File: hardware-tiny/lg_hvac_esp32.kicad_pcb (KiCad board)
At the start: 4 copper layers, 29 x 50.3 mm, 15 parts, among them J1 JST_XH_S3B-XH-A-1_01x03, J2 Conn_01x19_Female_1_to_19, J3 Conn_01x19_Female_20_to_38, U1 TPS82130, U2 TJA1027

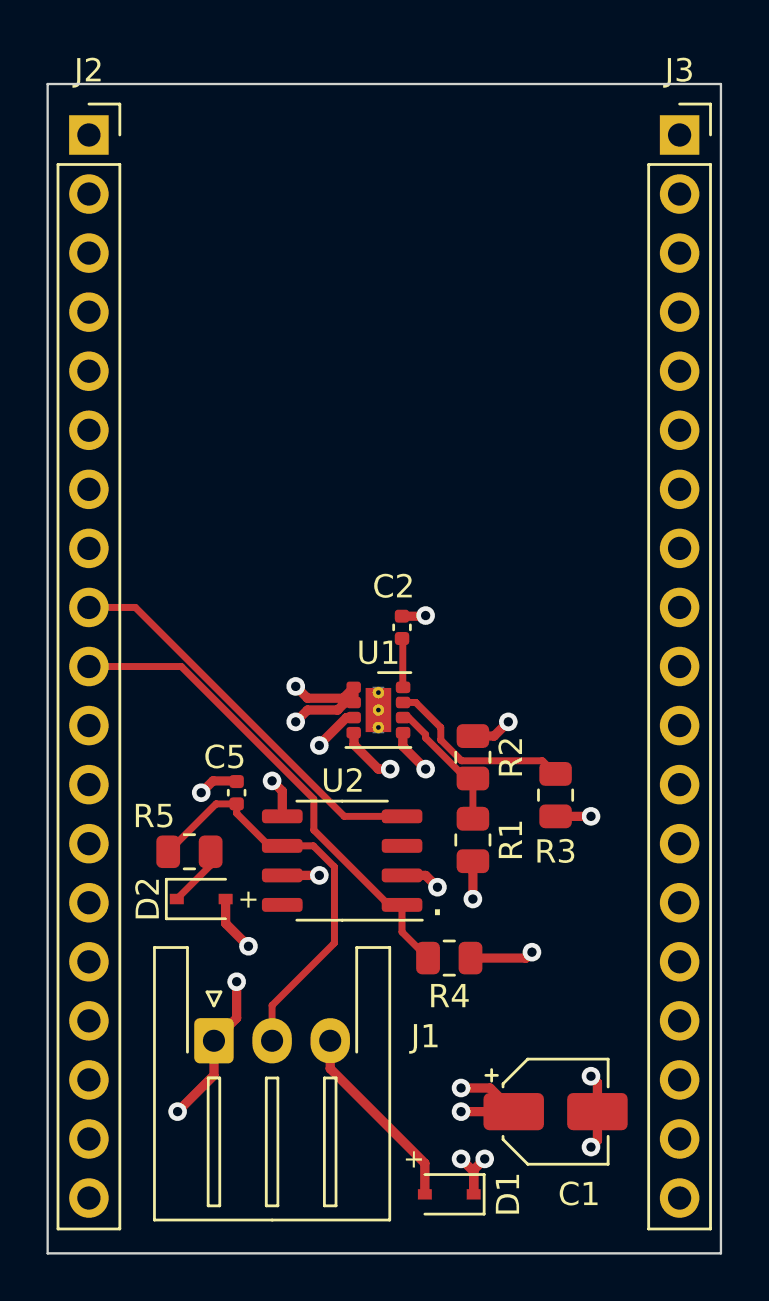
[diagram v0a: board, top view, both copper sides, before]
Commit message: Replaced C1 with a component that is available at jlcpcb.
Fixed all DRC errors and warnings.

Updated project files for KiCAD 9. I used the
https://github.com/Bouni/kicad-jlcpcb-tools plugin with some custom
rotation settings for J1, J2, and J3 because the KiCAD library and
jlcpcb disagree.
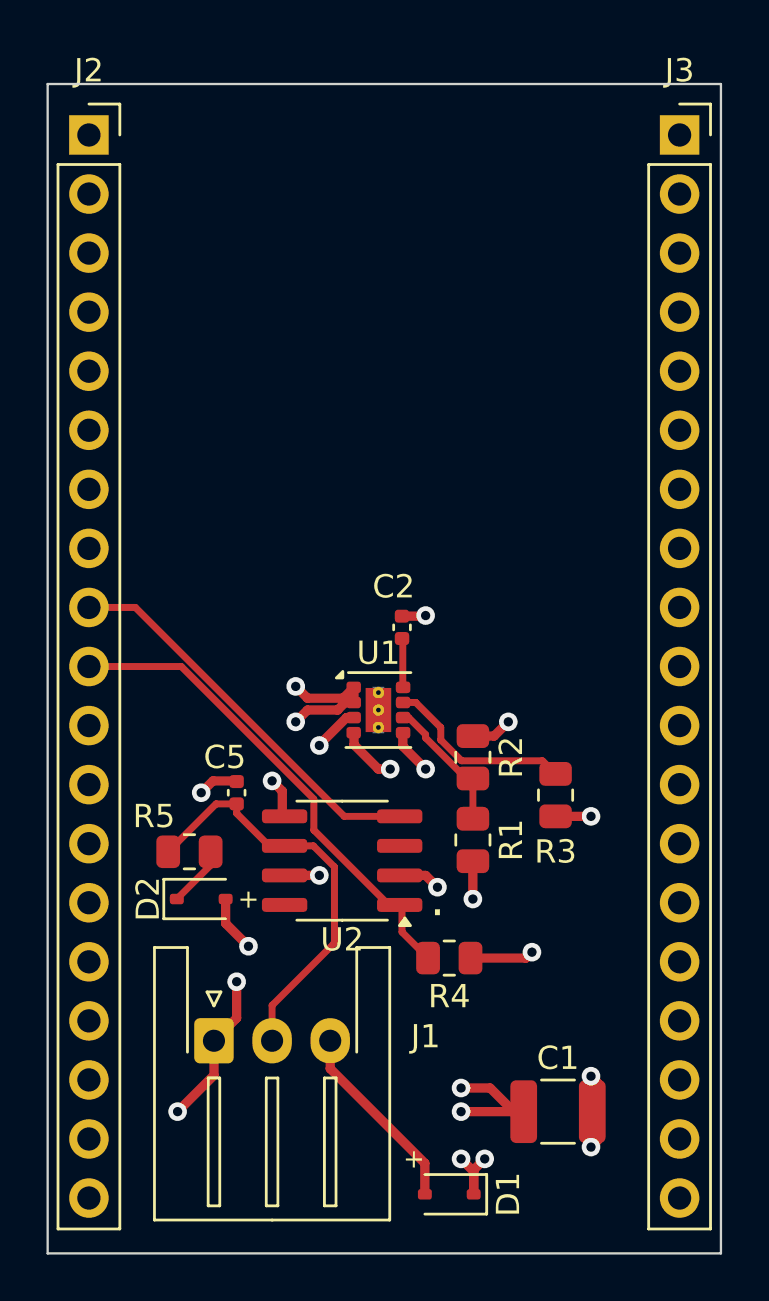
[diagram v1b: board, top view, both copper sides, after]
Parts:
- C1: footprint Capacitor_SMD:CP_Elec_4x5.4 -> Capacitor_SMD:C_1210_3225Metric
- U2: footprint Package_SO:SO-8_3.9x4.9mm_P1.27mm -> Package_SO:SOIC-8_3.9x4.9mm_P1.27mm
- moved C1 0.10 mm to (57.0, 76.7)
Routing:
- net +12V: track 18.9 -> 19.7 mm
